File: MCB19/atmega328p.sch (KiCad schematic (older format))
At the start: 22 parts, among them J401 USART, J402 DISABLE, U401 ATMEGA328P-PU, Y401 16MHz

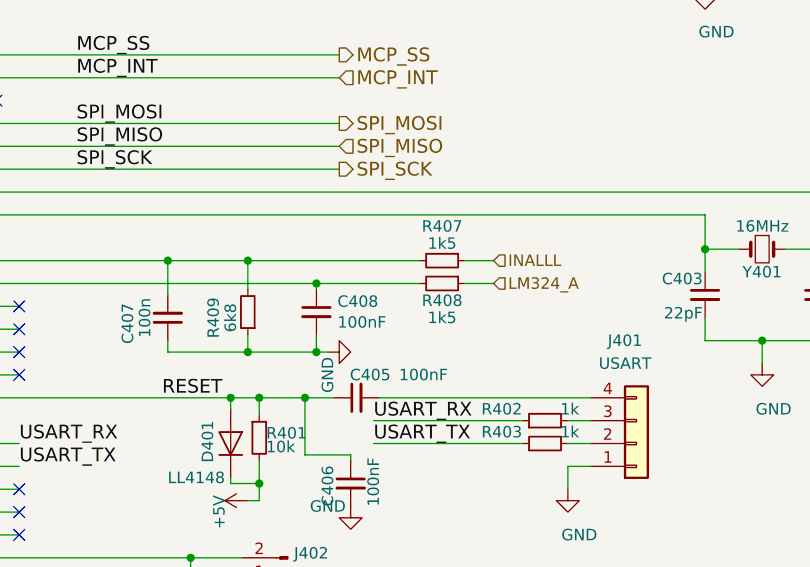
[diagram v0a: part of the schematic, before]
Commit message: Novos detalhes na placa
Comecei a planejar onde ficam os componentes da placa, em especial os que fazem parte do buck e os que estão no atmega328p, exceto os do driver
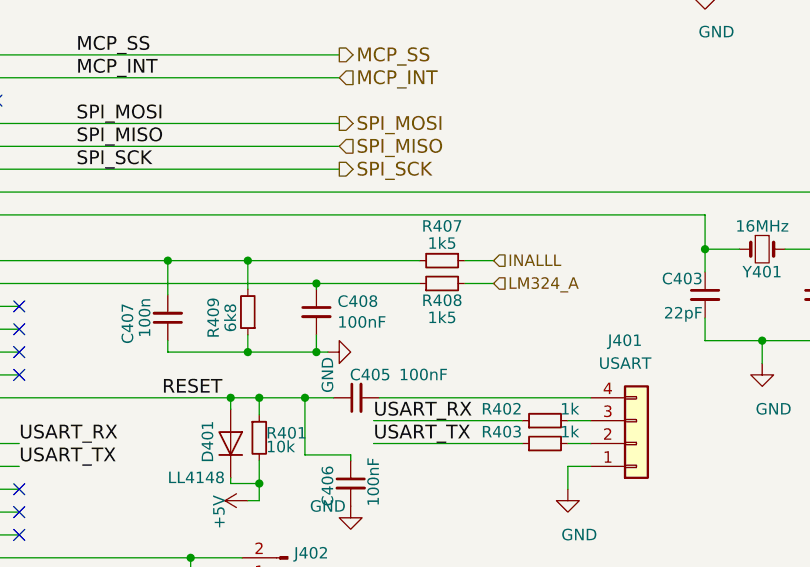
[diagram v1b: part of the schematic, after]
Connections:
- net LM324_A: now also R408.2; no longer R408.1
- net at C408.1, U401.24 (PC1): now also R408.1; no longer R408.2
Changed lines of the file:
@@
 EESchema Schematic File Version 4
 LIBS:MCB19-cache
-EELAYER 26 0
+EELAYER 29 0
 EELAYER END
 $Descr A4 11693 8268
@@
 U 1 1 5D4B9662
 P 6900 3750
-F 0 "R408" V 6975 3750 50  0000 C CNN
-F 1 "1k5" V 7050 3750 50  0000 C CNN
+F 0 "R408" V 6825 3750 50  0000 C CNN
+F 1 "1k5" V 6750 3750 50  0000 C CNN
 F 2 "Resistor_SMD:R_0805_2012Metric_Pad1.15x1.40mm_HandSolder" H 6900 3750 50  0001 C CNN
 F 3 "~" H 6900 3750 50  0001 C CNN
 	1    6900 3750
-	0    1    1    0
-$EndComp
-Wire Wire Line
-	7000 3750 7125 3750
+	0    -1   -1   0
+$EndComp
 Wire Wire Line
 	6300 4250 6100 4250
@@
 Wire Wire Line
 	4950 3750 6350 3750
-Wire Wire Line
-	6350 3750 6800 3750
-Connection ~ 6350 3750
 $Comp
 L power:GND #PWR0101
@@
 	6025 5725 5800 5725
 Connection ~ 5800 5725
+Wire Wire Line
+	7125 3750 7000 3750
+Wire Wire Line
+	6800 3750 6350 3750
+Connection ~ 6350 3750
 $EndSCHEMATC

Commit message: Final
Design de layout pronto
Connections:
- net PWM: now also U401.28 (PC5); no longer U401.12 (PD6)
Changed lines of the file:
@@
 GND
-$Comp
-L MCU_Microchip_ATmega:ATmega328P-PU U401
-U 1 1 59FE3414
-P 4350 3950
-F 0 "U401" H 3850 5400 50  0000 L BNN
-F 1 "ATMEGA328P-PU" H 4500 2450 50  0000 L BNN
-F 2 "Package_DIP:DIP-28_W7.62mm_Socket" H 4350 3950 50  0001 C CIN
-F 3 "" H 4350 3950 50  0001 C CNN
-	1    4350 3950
-	1    0    0    -1
-$EndComp
 $Comp
 L Device:R_Small R402
@@
 NoConn ~ 5050 3950
 NoConn ~ 5050 4050
-NoConn ~ 5050 4150
 NoConn ~ 5050 4650
 NoConn ~ 5050 4750
@@
 Text HLabel 7125 3750 2    50   Input ~ 0
 LM324_A
-Text HLabel 5100 5050 2    50   Output ~ 0
+Text HLabel 5050 4150 2    50   Output ~ 0
 PWM
-Wire Wire Line
-	4950 5050 5100 5050
 $Comp
 L Device:R_Small R407
@@
 	0    -1   -1   0
 $EndComp
+NoConn ~ 5050 5050
+$Comp
+L MCU_Microchip_ATmega:ATmega328P-PU U401
+U 1 1 59FE3414
+P 4350 3950
+F 0 "U401" H 3850 5400 50  0000 L BNN
+F 1 "ATMEGA328P-PU" H 4500 2450 50  0000 L BNN
+F 2 "Package_DIP:DIP-28_W7.62mm_Socket" H 4350 3950 50  0001 C CIN
+F 3 "" H 4350 3950 50  0001 C CNN
+	1    4350 3950
+	1    0    0    -1
+$EndComp
+Wire Wire Line
+	5050 5050 4950 5050
 $EndSCHEMATC

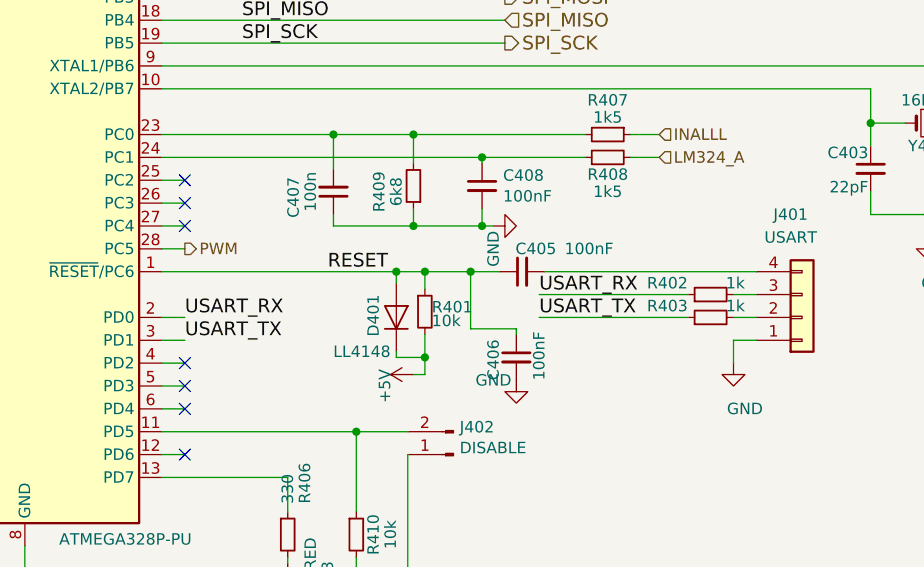
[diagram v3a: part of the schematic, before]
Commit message: Mudança nas trilhas para melhor funcionamento
Detalhes finais para a fabricação
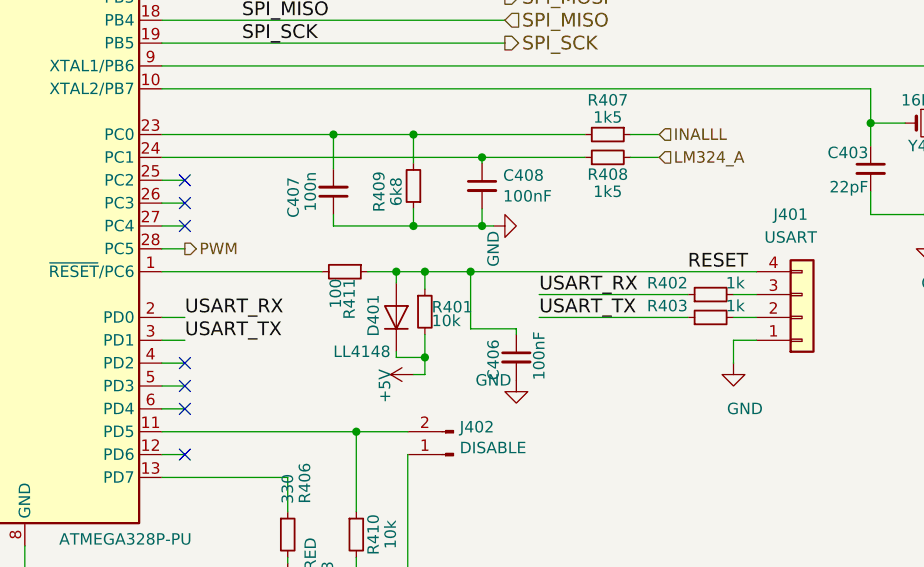
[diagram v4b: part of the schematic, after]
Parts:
- removed C405: 100nF, Capacitor_SMD:C_0805_2012Metric_Pad1.15x1.40mm_HandSolder, symbol Device:C_Small
- added R411: 100, Resistor_SMD:R_0805_2012Metric_Pad1.15x1.40mm_HandSolder, symbol Device:R_Small
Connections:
- net RESET: now also J401.4 (Pin_4), R411.1; no longer U401.1 (~RESET~/PC6)
- new net: R411.2, U401.1 (~RESET~/PC6)
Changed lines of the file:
@@
 EESchema Schematic File Version 4
 LIBS:MCB19-cache
-EELAYER 29 0
+EELAYER 26 0
 EELAYER END
 $Descr A4 11693 8268
@@
 Text HLabel 6450 2850 2    60   Input ~ 0
 MCP_INT
-Text Label 5675 4250 0    60   ~ 0
+Text Label 7250 4250 0    60   ~ 0
 RESET
 Text HLabel 7950 2200 0    60   Input ~ 0
@@
 	1    0    0    -1
 $EndComp
-$Comp
-L Device:C_Small C405
-U 1 1 5BED8033
-P 6525 4250
-F 0 "C405" V 6625 4100 50  0000 L CNN
-F 1 "100nF" V 6625 3850 50  0000 L CNN
-F 2 "Capacitor_SMD:C_0805_2012Metric_Pad1.15x1.40mm_HandSolder" H 6525 4250 50  0001 C CNN
-F 3 "" H 6525 4250 50  0001 C CNN
-	1    6525 4250
-	0    -1   -1   0
-$EndComp
 Text Label 5050 4450 0    60   ~ 0
 USART_RX
-Wire Wire Line
-	6625 4250 7550 4250
 $Comp
 L power:GND #PWR0409
@@
 	4950 5150 5500 5150
 Wire Wire Line
-	6300 4250 6425 4250
-Wire Wire Line
-	4950 4250 5975 4250
+	4950 4250 5650 4250
 Connection ~ 6300 4250
 Connection ~ 5975 4250
@@
 Wire Wire Line
 	5050 5050 4950 5050
+Wire Wire Line
+	6300 4250 7550 4250
+$Comp
+L Device:R_Small R411
+U 1 1 5D608202
+P 5750 4250
+F 0 "R411" H 5780 4270 50  0000 L CNN
+F 1 "100" H 5780 4210 50  0000 L CNN
+F 2 "Resistor_SMD:R_0805_2012Metric_Pad1.15x1.40mm_HandSolder" H 5750 4250 50  0001 C CNN
+F 3 "" H 5750 4250 50  0001 C CNN
+	1    5750 4250
+	0    1    1    0
+$EndComp
+Wire Wire Line
+	5850 4250 5975 4250
 $EndSCHEMATC
